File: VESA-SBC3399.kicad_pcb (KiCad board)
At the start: 2 copper layers, 12 parts

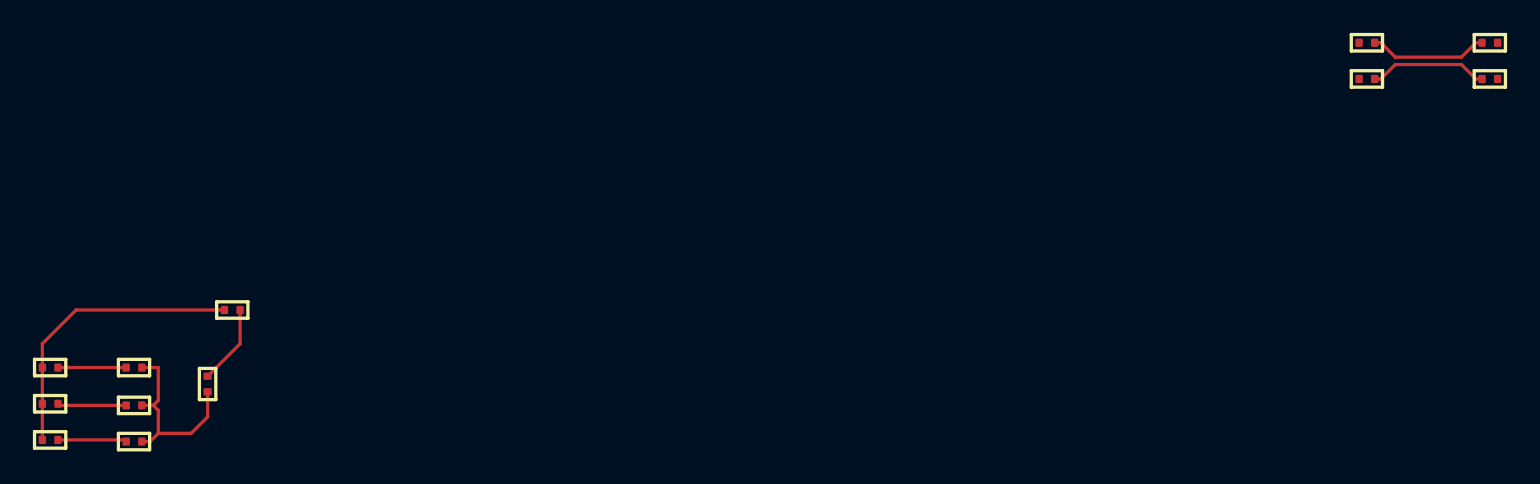
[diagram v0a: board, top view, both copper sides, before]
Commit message: create netclass
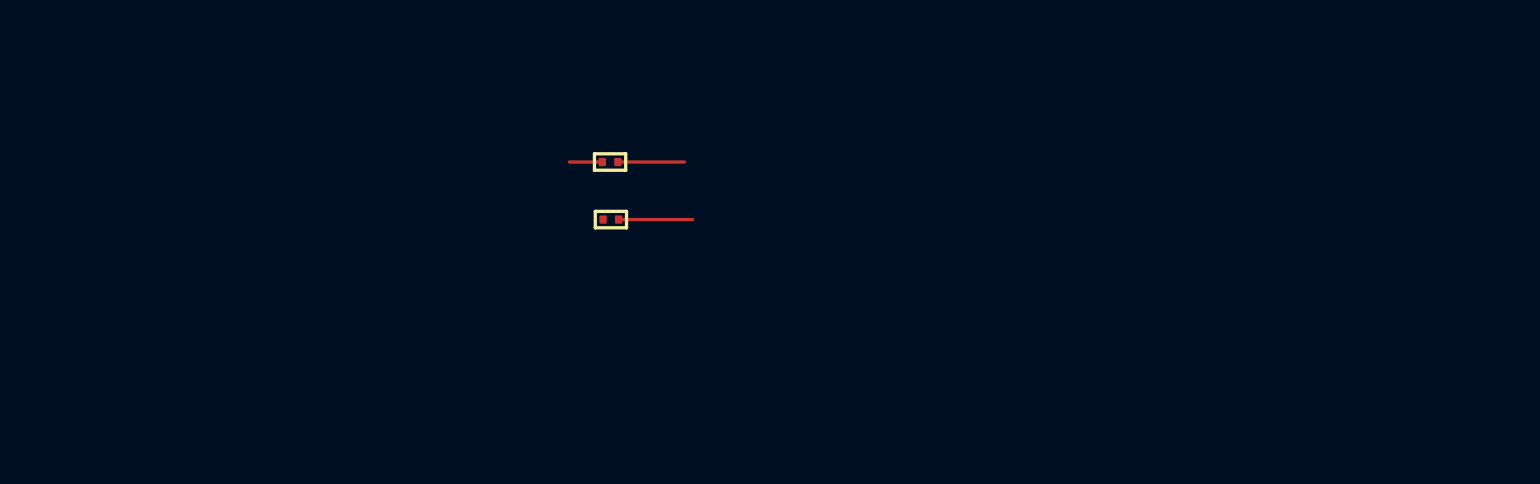
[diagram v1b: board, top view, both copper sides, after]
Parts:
- removed the R1 at (130.0, 118.0)
- removed the R1 at (208.0, 97.2)
- removed the R2 at (208.0, 99.4)
- removed the R2 at (131.5, 113.5)
- removed R3 (x2), R4 (x2), R5, R6, R7, R8: ~, footprints:RESC1005X35N
- added R1: ~, footprints:RESC1005X35N, F.Cu at (154.5, 104.5)
- added R2: ~, footprints:RESC1005X35N, F.Cu at (154.5, 108.0)
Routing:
- net Net-(R2-Pad1): track 17.8 -> 0.00 mm
- net Net-(R1-Pad2): track 12.1 -> 0.00 mm
- net /PCIe_REFCLK-: track 7.25 -> 0.00 mm
- net /PCIe_REFCLK+: track 7.25 -> 0.00 mm
- net /CPU-RK3399/PCIe: track 4.84 -> 0.00 mm
- net /USBC0_D+: track 0.00 -> 4.50 mm
- net /data2: track 4.19 -> 0.00 mm
- net /data1: track 4.19 -> 0.00 mm
- net /data0: track 4.15 -> 0.00 mm
- net /USBC0_INT#: track 0.00 -> 4.05 mm
- net /USBC1_INT#: track 0.00 -> 2.00 mm
